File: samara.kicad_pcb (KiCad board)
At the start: 2 copper layers, 30.5 x 30.5 mm, 55 parts, among them J1 CONN_02JST-PTH-2, J2 U.FL, J3 I2C_STANDARDQWIIC, P1 USB_C_Plug_USB2.0, Q1 DMG3418L, U1 RP2040, U2 BNO055, U3 BME280, U4 W25Q16JVSNIQ, U5 RFM95W-915S2, U6 MCP73831, U7 AP2112K-3.3, Y1 CRYSTAL-12MHZ", Y2 CRYSTAL-32.768KHZSMD-3.2X1.5

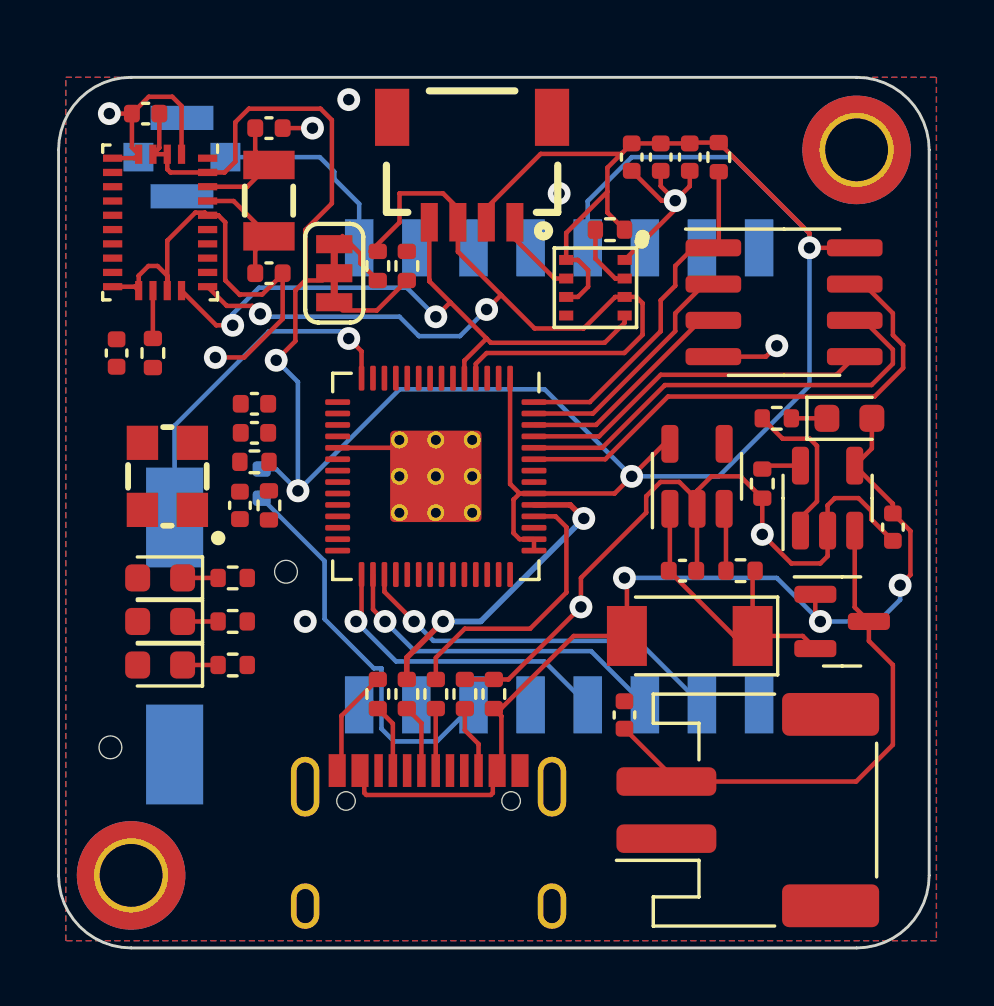
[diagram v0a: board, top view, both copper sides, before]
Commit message: updated IMU to BMI085
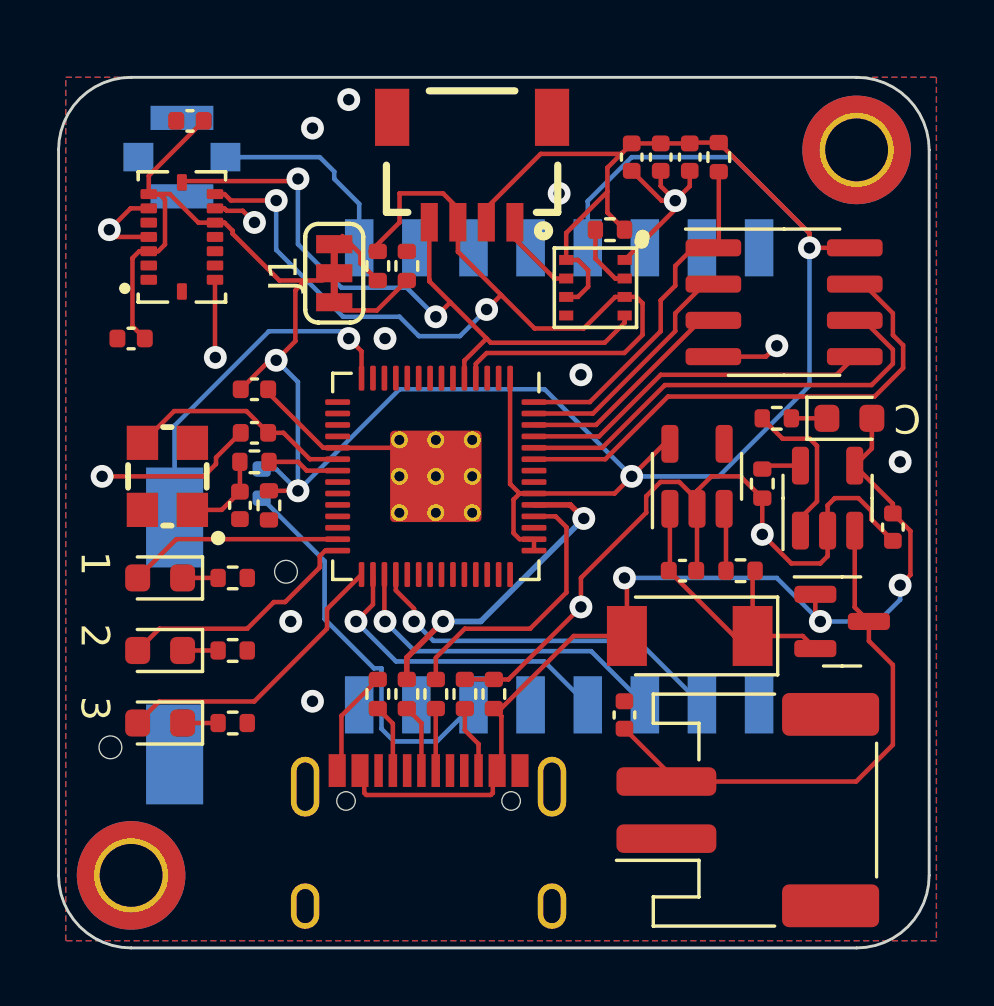
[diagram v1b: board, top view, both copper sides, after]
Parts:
- removed C10, C13: 22pF, Capacitor_SMD:C_0402_1005Metric
- removed R16: 10K, Resistor_SMD:R_0402_1005Metric
- removed Y2: CRYSTAL-32.768KHZSMD-3.2X1.5, Clocks:CRYSTAL-SMD-3.2X1.5MM
- U2: value BNO055 -> BMI085; footprint Package_LGA:LGA-28_5.2x3.8mm_P0.5mm -> BMI085:PQFN50P450X300X100-16N
- moved D4 2.54 mm to (133.1, 129.3)
- moved R15 2.54 mm to (135.6, 129.3)
- moved D5 2.03 mm to (133.1, 131.8)
- moved R20 2.03 mm to (135.6, 131.8)
- moved C6 1.57 mm to (134.1, 110.7)
- moved D3 1.52 mm to (133.1, 126.7)
- moved R12 1.52 mm to (135.6, 126.7)
- moved U2 0.92 mm to (133.9, 114.8), turned to 90 degrees
- moved C9 0.72 mm to (132.1, 118.4), turned to 180 degrees
- moved C8 0.51 mm to (136.4, 120.1)
- turned C2 to 0 degrees
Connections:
- C8 pad 1: GND -> +3V3
- C8 pad 2: +3V3 -> GND
- C9 pad 1: Net-(C9-Pad1) -> +3V3
- D5 pad 2: unconnected-(D5-Pad2) -> /LED3
- U1 pad 29: /SCK -> /LED3
- U1 pad 30: /PICO -> /SCK
- U1 pad 31: /POCI -> /PICO
- U1 pad 32: unconnected-(U1-Pad32) -> /POCI
- U2 pad 11: /IMURST -> +3V3
- U2 pad 14: /INT -> unconnected-(U2-Pad14)
- U2 pad 16: GND -> unconnected-(U2-Pad16)
- U2 pad 2: GND -> (no net)
- U2 pad 4: +3V3 -> GND
- U2 pad 5: GND -> unconnected-(U2-Pad5)
- U2 pad 7: unconnected-(U2-Pad7) -> +3V3
- U2 pad 8: unconnected-(U2-Pad8) -> /SCL
- U2 pad 9: Net-(C9-Pad1) -> /SDA
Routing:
- net /LED3: track 0.00 -> 10.4 mm
- net /LED2: track 0.00 -> 8.68 mm
- net GND: track 70.3 -> 61.9 mm, vias 10 -> 16
- net Net-(C2-Pad2): track 0.00 -> 8.02 mm
- net /LED1: track 0.00 -> 7.56 mm
- net Net-(C10-Pad1): track 4.15 -> 0.00 mm
- net Net-(C13-Pad1): track 3.95 -> 0.00 mm
- net +3V3: track 102.5 -> 105.6 mm
- net Net-(C1-Pad2): track 0.00 -> 2.98 mm
- net Net-(R2-Pad2): track 0.00 -> 2.53 mm
- net /SDA: track 33.8 -> 35.9 mm
- net /SCL: track 23.4 -> 25.0 mm
- net Net-(U2-Pad17): track 1.68 -> 0.00 mm
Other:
- board text added: "1"
- board text added: "2"
- board text added: "3"
- board text added: "C"
- board text added: "J1"

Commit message: update 3d models
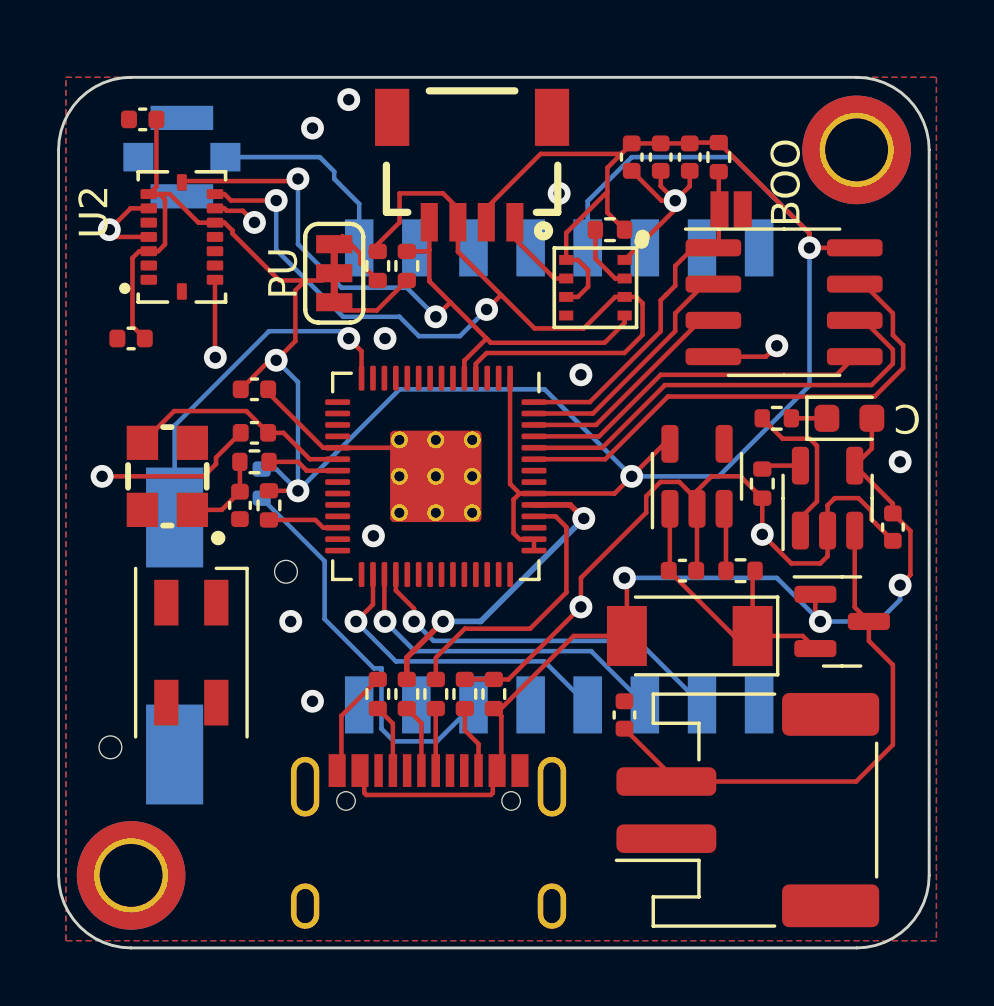
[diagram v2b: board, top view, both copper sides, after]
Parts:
- removed D4, D5: LED, LED_SMD:LED_0603_1608Metric
- removed R12, R15, R20: 10K, Resistor_SMD:R_0402_1005Metric
- added JP2: SolderJumper_2_Open, Jumpers:SMT-JUMPER_2_NO_NO-SILK, F.Cu at (153.1, 113.8)
- D3: value LED -> SK6812MINI; footprint LED_SMD:LED_0603_1608Metric -> LED_SMD:LED_SK6812MINI_PLCC4_3.5x3.5mm_P1.75mm
- moved D3 2.84 mm to (134.2, 129.4), turned to 90 degrees
- moved C6 1.65 mm to (132.5, 110.7)
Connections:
- D3 pad 1: Net-(D3-Pad1) -> unconnected-(D3-Pad1)
- D3 pad 2: /LED1 -> unconnected-(D3-Pad2)
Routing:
- net /LED3: track 10.4 -> 0.00 mm
- net /LED2: track 8.68 -> 0.00 mm
- net /LED1: track 7.56 -> 0.00 mm
- net Net-(R1-Pad2): track 0.00 -> 2.52 mm
- net Net-(D5-Pad1): track 1.24 -> 0.00 mm
- net Net-(D4-Pad1): track 1.24 -> 0.00 mm
- net Net-(D3-Pad1): track 1.24 -> 0.00 mm
- net /SCL: track 25.0 -> 25.9 mm
- net +3V3: track 105.6 -> 105.0 mm
- net (no net): vias 0 -> 1
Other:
- board text added: "BOO"
- board text added: "PU"
- board text removed: "1"
- board text removed: "2"
- board text removed: "3"
- board text removed: "J1"

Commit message: assorted updates and 3d models
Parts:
- added J4: CONN_01, Connectors:1X01_NO_SILK, F.Cu at (137.4, 112.0)
- added J5: CONN_02, Connectors:1X02, F.Cu at (134.0, 120.0)
- D3: value SK6812MINI -> SK6805; footprint LED_SMD:LED_SK6812MINI_PLCC4_3.5x3.5mm_P1.75mm -> LED_SMD:LED_SK6805_PLCC4_2.4x2.7mm_P1.3mm
- U7: value AP2112K-3.3 -> LDS3985M33R
- moved C9 2.50 mm to (131.1, 116.1), turned to -90 degrees
- moved Y1 1.80 mm to (133.1, 125.0)
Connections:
- D3 pad 2: unconnected-(D3-Pad2) -> GND
- D3 pad 3: unconnected-(D3-Pad3) -> /LED1
- D3 pad 4: unconnected-(D3-Pad4) -> +3V3
- J2 pad 1: unconnected-(J2-Pad1) -> GND
- J2 pad 2: unconnected-(J2-Pad2) -> GND
- U1 pad 28: /LED2 -> unconnected-(U1-Pad28)
- U1 pad 29: /LED3 -> unconnected-(U1-Pad29)
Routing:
- net Net-(R1-Pad2): track 2.52 -> 17.6 mm
- net +3V3: track 105.0 -> 113.4 mm, vias 4 -> 5
- net /LED1: track 0.00 -> 5.82 mm
- net Net-(C1-Pad2): track 2.98 -> 4.54 mm
- net Net-(C2-Pad2): track 8.02 -> 9.29 mm
- net /SCL: track 25.9 -> 24.9 mm
- net GND: track 61.9 -> 61.8 mm, vias 16 -> 28
- net (no net): vias 1 -> 0
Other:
- outline, holes or cut-outs redrawn
- board text added: "B"
- board text removed: "BOO"

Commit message: close to v1 production
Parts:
- added J6: CONN_03, Connectors:1X03, F.Cu at (148.6, 111.0)
- C11, C12, C5: moved to B.Cu
- J2: value U.FL -> CON-SMA-EDGE-S; footprint Connectors:U.FL -> CON-SMA-EDGE-S:RFSOLUTIONS_CON-SMA-EDGE-S
- J4: value CONN_01 -> U.FL; footprint Connectors:1X01_NO_SILK -> Connectors:U.FL; moved to B.Cu
- moved C5 9.80 mm to (157.5, 117.9), turned to 0 degrees
- moved C12 8.24 mm to (157.5, 116.6), turned to 180 degrees
- moved C6 8.17 mm to (137.1, 117.4), turned to -90 degrees
- moved C11 6.71 mm to (157.5, 115.3), turned to 180 degrees
- moved J4 4.80 mm to (134.1, 115.4), turned to 90 degrees
- moved R3 2.27 mm to (154.1, 113.7), turned to 180 degrees
- moved C9 2.04 mm to (130.9, 118.1)
- moved U2 2.04 mm to (133.7, 116.8)
- moved R18 1.64 mm to (141.0, 117.3), turned to 180 degrees
- moved J2 1.63 mm to (135.1, 111.0), turned to -90 degrees
- moved U3 1.37 mm to (148.8, 115.3)
- moved R14 1.31 mm to (149.1, 113.3)
- moved D3 1.27 mm to (134.2, 130.6)
- moved JP2 1.00 mm to (152.1, 113.7), turned to 0 degrees
- moved J5 0.90 mm to (133.9, 120.9)
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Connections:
- J2 pad 1: GND -> Net-(J2-Pad1)
- J4 pad 1: Net-(J2-PadFEED) -> GND
- U5 pad 9: Net-(J2-PadFEED) -> Net-(J2-Pad1)
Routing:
- net /TX: track 0.00 -> 14.4 mm, vias 0 -> 1
- net /RX: track 0.00 -> 13.8 mm, vias 0 -> 1
- net +3V3: track 113.4 -> 101.0 mm
- net Net-(J2-Pad1): track 0.00 -> 9.69 mm
- net GND: track 61.8 -> 53.8 mm, vias 28 -> 35
- net Net-(J2-PadFEED): track 7.20 -> 0.00 mm
- net /SDA: track 35.6 -> 29.2 mm
- net /SCL: track 24.9 -> 27.3 mm, vias 2 -> 3
- net Net-(JP1-Pad3): track 2.69 -> 1.16 mm
- net /LED1: track 5.82 -> 6.78 mm
- net Net-(JP1-Pad1): track 2.07 -> 1.13 mm
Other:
- board text added: "A"
- board text added: "samara v1.0 Red Wolf Space Program"
- board text removed: "B"
- board text removed: "C"
- board text removed: "PU"
- board text removed: "samara v0.1 Red Wolf Space Program"

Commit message: ready for first pcb fab
get ready for bodges...
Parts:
- added C10: 0.1uF, Capacitor_SMD:C_0402_1005Metric, F.Cu at (134.4, 133.1)
- added C13: 0.1uF, Capacitor_SMD:C_0402_1005Metric, B.Cu at (157.2, 122.7)
- added C14: 0.1uF, Capacitor_SMD:C_0402_1005Metric, F.Cu at (132.1, 128.5)
- added C15: 0.1uF, Capacitor_SMD:C_0402_1005Metric, B.Cu at (157.2, 123.7)
- added C16: 0.1uF, Capacitor_SMD:C_0402_1005Metric, F.Cu at (132.1, 130.6)
- added C17: 2.2uF, Capacitor_SMD:C_0402_1005Metric, B.Cu at (157.2, 121.7)
- added C18: 0.1uF, Capacitor_SMD:C_0402_1005Metric, F.Cu at (132.1, 129.5)
- added C19: 0.1uF, Capacitor_SMD:C_0402_1005Metric, F.Cu at (132.9, 131.6)
- added C20: 0.1uF, Capacitor_SMD:C_0402_1005Metric, F.Cu at (132.9, 132.6)
- added C21: 0.1uF, Capacitor_SMD:C_0402_1005Metric, F.Cu at (132.9, 133.6)
- added C22: 2.2uF, Capacitor_SMD:C_0402_1005Metric, F.Cu at (132.1, 127.5)
- added C23: 2.2uF, Capacitor_SMD:C_0402_1005Metric, B.Cu at (157.2, 126.0)
- added R12: 10K, Resistor_SMD:R_0402_1005Metric, B.Cu at (157.2, 127.0)
- moved C1 3.08 mm to (133.8, 126.5), turned to 180 degrees
- moved J5 2.55 mm to (131.3, 121.2), turned to 0 degrees
- moved R13 2.34 mm to (138.2, 125.2)
- moved D3 1.69 mm to (135.6, 129.8)
- moved J4 1.57 mm to (133.3, 116.8)
- moved J2 1.55 mm to (134.9, 112.5)
- moved C3 1.29 mm to (148.1, 131.3)
- moved R2 1.08 mm to (137.2, 123.4)
- moved R1 1.05 mm to (137.2, 125.2), turned to 0 degrees
- moved Y1 0.92 mm to (133.6, 124.2), turned to 0 degrees
- moved C2 0.56 mm to (136.9, 121.9), turned to -90 degrees
- moved U2 0.53 mm to (133.9, 117.3)
- moved C8 0.25 mm to (136.7, 120.4)
- turned JP2 to 180 degrees
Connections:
- JP2 pad 1: GND -> /QSPI_CS
- JP2 pad 2: /QSPI_CS -> GND
- U1 pad 23: unconnected-(U1-Pad23) -> +1V2
- U1 pad 28: unconnected-(U1-Pad28) -> /RST
- U1 pad 29: unconnected-(U1-Pad29) -> /NSS
- U1 pad 43: +3V3 -> Net-(U1-Pad43)
- U1 pad 45: unconnected-(U1-Pad45) -> +1V2
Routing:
- net +3V3: track 101.0 -> 129.5 mm
- net +1V2: track 0.00 -> 23.1 mm, vias 0 -> 1
- net GND: track 53.8 -> 74.7 mm, vias 35 -> 38
- net Net-(U1-Pad43): track 0.00 -> 12.2 mm, vias 0 -> 1
- net Net-(J5-Pad2): track 17.3 -> 7.72 mm, vias 0 -> 2
- net /NSS: track 0.00 -> 9.51 mm, vias 0 -> 1
- net Net-(C2-Pad2): track 9.29 -> 4.13 mm
- net Net-(C1-Pad2): track 4.54 -> 6.69 mm
- net /LED1: track 6.78 -> 5.15 mm
- net +BATT: track 19.0 -> 20.3 mm
- net Net-(J2-Pad1): track 9.69 -> 10.6 mm
- net /SCK: track 11.2 -> 10.3 mm
- net Net-(R2-Pad2): track 2.53 -> 1.83 mm
- net /D+: track 10.9 -> 11.5 mm
- net /RST: track 14.2 -> 14.5 mm, vias 0 -> 1
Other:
- board text removed: "A"
